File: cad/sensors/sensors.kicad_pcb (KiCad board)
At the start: 2 copper layers, 72 x 50 mm, 4 parts

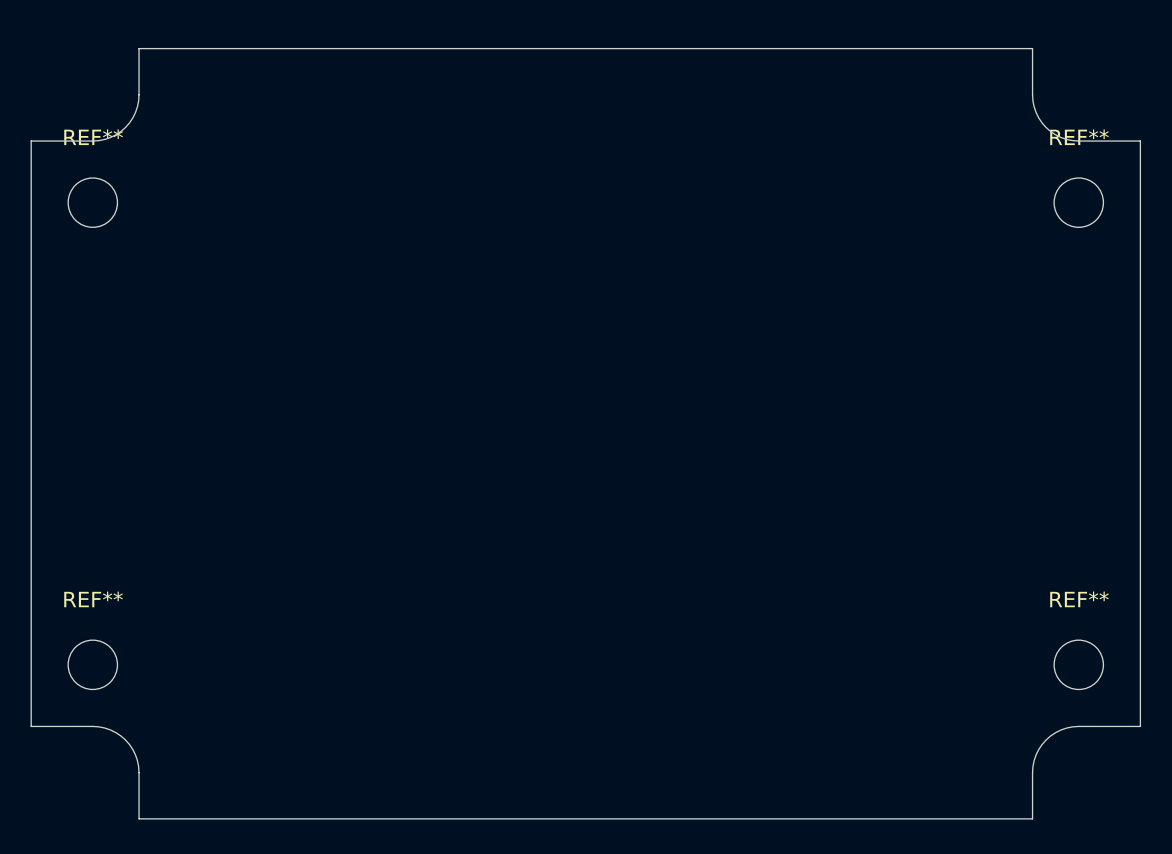
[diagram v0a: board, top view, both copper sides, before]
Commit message: Finished sensor breakout board placement. Ready to begin routing
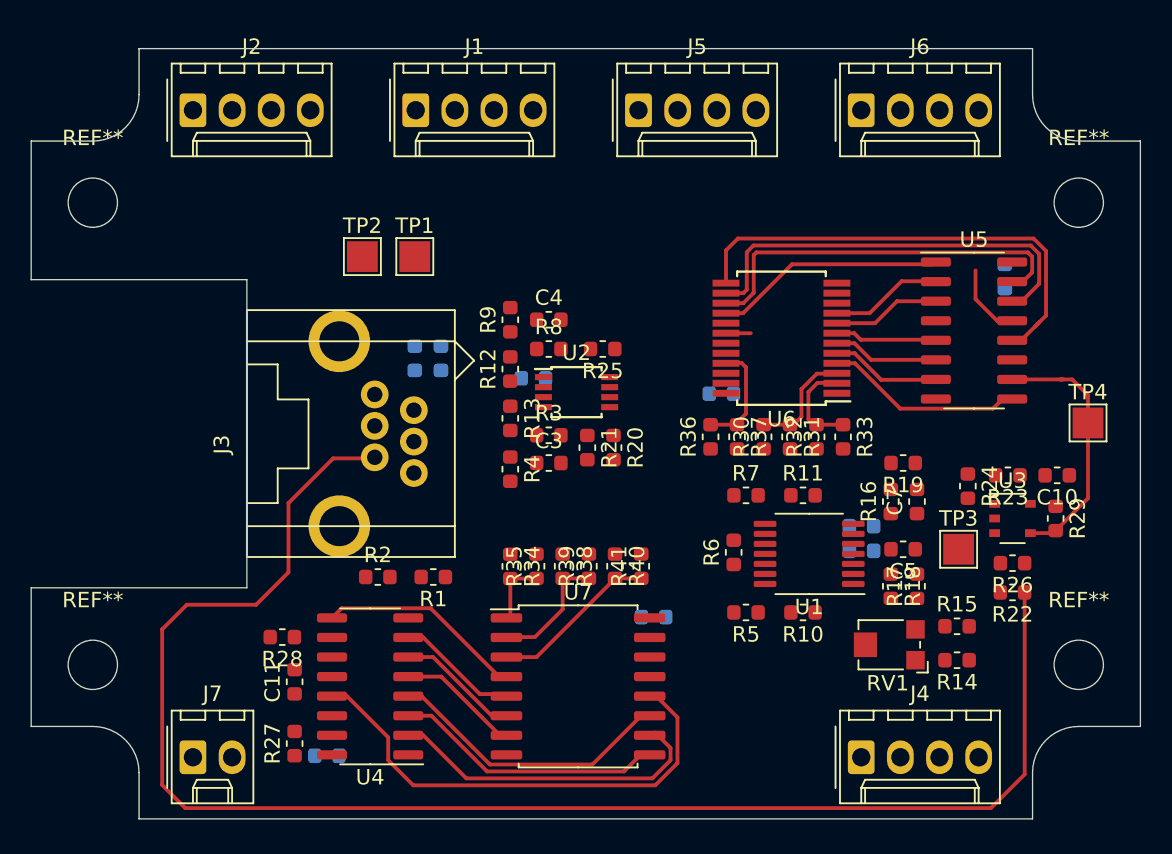
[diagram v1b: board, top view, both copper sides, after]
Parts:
- added C1: 10uF, Capacitor_SMD:C_0603_1608Metric, B.Cu at (120.8, 85.2)
- added C10: 100nF, Capacitor_SMD:C_0603_1608Metric, F.Cu at (162.5, 92.8)
- added C11: 100nF, Capacitor_SMD:C_0603_1608Metric, F.Cu at (113.0, 106.2)
- added C12: 100nF, Capacitor_SMD:C_0603_1608Metric, B.Cu at (140.7, 87.5)
- added C13: 100nF, Capacitor_SMD:C_0603_1608Metric, B.Cu at (115.1, 111.0)
- added C14: 100nF, Capacitor_SMD:C_0603_1608Metric, B.Cu at (136.3, 102.0)
- added C15: 100nF, Capacitor_SMD:C_0603_1608Metric, B.Cu at (159.1, 79.8)
- added C2: 100nF, Capacitor_SMD:C_0603_1608Metric, B.Cu at (122.5, 85.2)
- added C3: DNF, Capacitor_SMD:C_0603_1608Metric, F.Cu at (129.5, 92.0)
- added C4: DNF, Capacitor_SMD:C_0603_1608Metric, F.Cu at (129.5, 82.7)
- added C5: 4.7uF, Capacitor_SMD:C_0603_1608Metric, F.Cu at (152.5, 97.5)
- added C6: 100nF, Capacitor_SMD:C_0603_1608Metric, B.Cu at (128.5, 86.5)
- added C7: 100nF, Capacitor_SMD:C_0603_1608Metric, F.Cu at (153.4, 94.5)
- added C8: 10nF, Capacitor_SMD:C_0603_1608Metric, B.Cu at (149.8, 97.7)
- added C9: 1uF, Capacitor_SMD:C_0603_1608Metric, B.Cu at (149.8, 96.0)
- added J1: Conn_01x04, Connector_Molex:Molex_KK-254_AE-6410-04A_1x04_P2.54mm_Vertical, F.Cu at (120.9, 69.0)
- added J2: Conn_01x04, Connector_Molex:Molex_KK-254_AE-6410-04A_1x04_P2.54mm_Vertical, F.Cu at (106.4, 69.0)
- added J3: 6P6C, custom:E5566-Q0LK22-L, F.Cu at (115.9, 84.0)
- added J4: Conn_01x04, Connector_Molex:Molex_KK-254_AE-6410-04A_1x04_P2.54mm_Vertical, F.Cu at (149.8, 111.0)
- added J5: Conn_01x04, Connector_Molex:Molex_KK-254_AE-6410-04A_1x04_P2.54mm_Vertical, F.Cu at (135.3, 69.0)
- added J6: Conn_01x04, Connector_Molex:Molex_KK-254_AE-6410-04A_1x04_P2.54mm_Vertical, F.Cu at (149.8, 69.0)
- added J7: Conn_01x02, Connector_Molex:Molex_KK-254_AE-6410-02A_1x02_P2.54mm_Vertical, F.Cu at (106.4, 111.0)
- added R1: 0, Resistor_SMD:R_0603_1608Metric, F.Cu at (122.0, 99.3)
- added R10: 1k, Resistor_SMD:R_0603_1608Metric, F.Cu at (146.0, 101.7)
- added R11: 1k, Resistor_SMD:R_0603_1608Metric, F.Cu at (146.0, 94.0)
- added R12: 75, Resistor_SMD:R_0603_1608Metric, F.Cu at (127.0, 85.8)
- added R13: 75, Resistor_SMD:R_0603_1608Metric, F.Cu at (127.0, 89.0)
- added R14: 33k, Resistor_SMD:R_0603_1608Metric, F.Cu at (156.0, 104.8)
- added R15: 33k, Resistor_SMD:R_0603_1608Metric, F.Cu at (156.0, 102.5)
- added R16: 39k, Resistor_SMD:R_0603_1608Metric, F.Cu at (151.7, 94.5)
- added R17: 39k, Resistor_SMD:R_0603_1608Metric, F.Cu at (153.4, 100.0)
- added R18: 0, Resistor_SMD:R_0603_1608Metric, F.Cu at (151.7, 100.0)
- added R19: 1.6k, Resistor_SMD:R_0603_1608Metric, F.Cu at (152.5, 92.0)
- added R2: DNF, Resistor_SMD:R_0603_1608Metric, F.Cu at (118.4, 99.3)
- added R20: 10k, Resistor_SMD:R_0603_1608Metric, F.Cu at (133.7, 91.0)
- added R21: 10k, Resistor_SMD:R_0603_1608Metric, F.Cu at (132.0, 91.0)
- added R22: DNF, Resistor_SMD:R_0603_1608Metric, F.Cu at (159.6, 100.3)
- added R23: 100k, Resistor_SMD:R_0603_1608Metric, F.Cu at (159.3, 92.8)
- added R24: 100k, Resistor_SMD:R_0603_1608Metric, F.Cu at (156.7, 93.5)
- added R25: 10k, Resistor_SMD:R_0603_1608Metric, F.Cu at (133.0, 84.5)
- added R26: 775k, Resistor_SMD:R_0603_1608Metric, F.Cu at (159.6, 98.5)
- added R27: 10k, Resistor_SMD:R_0603_1608Metric, F.Cu at (113.0, 110.2)
- added R28: 100k, Resistor_SMD:R_0603_1608Metric, F.Cu at (112.2, 103.2)
- added R29: 10k, Resistor_SMD:R_0603_1608Metric, F.Cu at (162.4, 95.5)
- added R3: 2.2k, Resistor_SMD:R_0603_1608Metric, F.Cu at (129.5, 90.2)
- added R30: DNF, Resistor_SMD:R_0603_1608Metric, F.Cu at (143.4, 90.2)
- added R31: 0, Resistor_SMD:R_0603_1608Metric, F.Cu at (145.2, 90.2)
- added R32: DNF, Resistor_SMD:R_0603_1608Metric, F.Cu at (146.9, 90.2)
- added R33: 0, Resistor_SMD:R_0603_1608Metric, F.Cu at (148.6, 90.2)
- added R34: DNF, Resistor_SMD:R_0603_1608Metric, F.Cu at (127.0, 98.7)
- added R35: 0, Resistor_SMD:R_0603_1608Metric, F.Cu at (128.7, 98.7)
- added R36: DNF, Resistor_SMD:R_0603_1608Metric, F.Cu at (140.0, 90.2)
- added R37: 0, Resistor_SMD:R_0603_1608Metric, F.Cu at (141.7, 90.2)
- added R38: DNF, Resistor_SMD:R_0603_1608Metric, F.Cu at (130.4, 98.7)
- added R39: 0, Resistor_SMD:R_0603_1608Metric, F.Cu at (132.1, 98.7)
- added R4: DNF, Resistor_SMD:R_0603_1608Metric, F.Cu at (127.0, 92.3)
- added R40: DNF, Resistor_SMD:R_0603_1608Metric, F.Cu at (133.8, 98.7)
- added R41: 0, Resistor_SMD:R_0603_1608Metric, F.Cu at (135.5, 98.7)
- added R5: 0, Resistor_SMD:R_0603_1608Metric, F.Cu at (142.3, 101.7)
- added R6: DNF, Resistor_SMD:R_0603_1608Metric, F.Cu at (141.5, 97.8)
- added R7: 0, Resistor_SMD:R_0603_1608Metric, F.Cu at (142.3, 94.0)
- added R8: 2.2k, Resistor_SMD:R_0603_1608Metric, F.Cu at (129.5, 84.5)
- added R9: DNF, Resistor_SMD:R_0603_1608Metric, F.Cu at (127.0, 82.7)
- added RV1: 10k, Potentiometer_SMD:Potentiometer_Bourns_TC33X_Vertical, F.Cu at (151.5, 103.8)
- added TP1: RCU-0C, TestPoint:TestPoint_Pad_2.0x2.0mm, F.Cu at (120.8, 78.5)
- added TP2: RCU-0C, TestPoint:TestPoint_Pad_2.0x2.0mm, F.Cu at (117.4, 78.5)
- added TP3: RCU-0C, TestPoint:TestPoint_Pad_2.0x2.0mm, F.Cu at (156.1, 97.5)
- added TP4: RCU-0C, TestPoint:TestPoint_Pad_2.0x2.0mm, F.Cu at (164.5, 89.3)
- added U1: LMV324, Package_SO:TSSOP-14_4.4x5mm_P0.65mm, F.Cu at (146.4, 97.8)
- added U2: PCA9517A, Package_SO:TSSOP-8_3x3mm_P0.65mm, F.Cu at (131.3, 87.3)
- added U3: LMV331, Package_SO:TSOP-5_1.65x3.05mm_P0.95mm, F.Cu at (159.6, 95.5)
- added U4: MC14040B, Package_SO:SOIC-16_3.9x9.9mm_P1.27mm, F.Cu at (117.9, 106.5)
- added U5: MC14040B, Package_SO:SOIC-16_3.9x9.9mm_P1.27mm, F.Cu at (157.1, 83.3)
- added U6: TCA9555DBR, Package_SO:SSOP-24_5.3x8.2mm_P0.65mm, F.Cu at (144.6, 83.8)
- added U7: PCF8574, Package_SO:SOIC-16W_7.5x10.3mm_P1.27mm, F.Cu at (131.4, 106.5)
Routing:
- net /ADC: track 0.00 -> 100.4 mm
- net Net-(U4-Pad13): track 0.00 -> 31.4 mm
- net Net-(U5-Pad12): track 0.00 -> 30.5 mm
- net Net-(U5-Pad14): track 0.00 -> 26.9 mm
- net Net-(U5-Pad15): track 0.00 -> 24.8 mm
- net Net-(U4-Pad2): track 0.00 -> 20.9 mm
- net Net-(U4-Pad4): track 0.00 -> 18.1 mm
- net Net-(U4-Pad3): track 0.00 -> 16.9 mm
- net Net-(R26-Pad1): track 0.00 -> 16.1 mm
- net Net-(U5-Pad1): track 0.00 -> 14.7 mm
- net Net-(U4-Pad9): track 0.00 -> 13.1 mm
- net Net-(U5-Pad9): track 0.00 -> 12.3 mm
- net Net-(R40-Pad2): track 0.00 -> 10.8 mm
- net Net-(U4-Pad6): track 0.00 -> 8.14 mm
- net Net-(U4-Pad7): track 0.00 -> 8.05 mm
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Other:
- outline, holes or cut-outs redrawn

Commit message: Finished routing sensor breakout board. Need to draw power planes
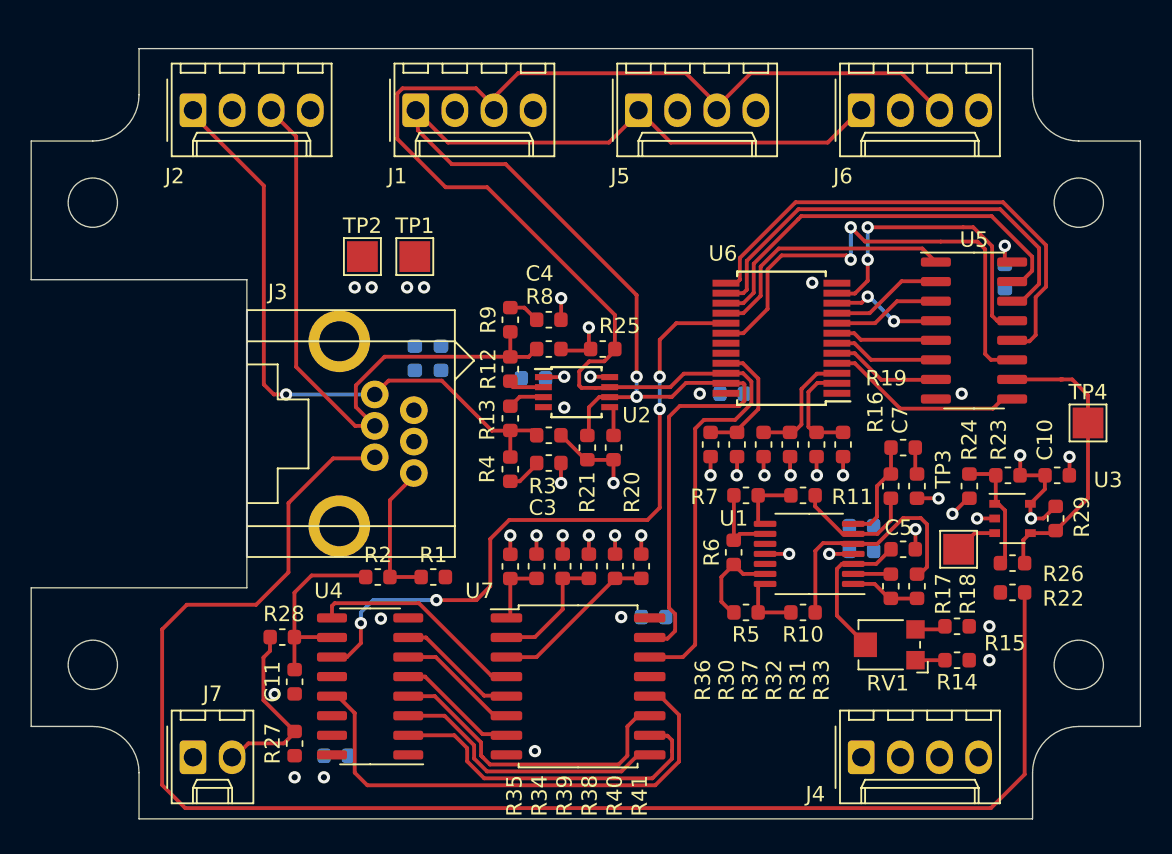
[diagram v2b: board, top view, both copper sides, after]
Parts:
- moved C7 1.00 mm to (153.4, 93.5)
- moved R16 1.00 mm to (151.7, 93.5)
- moved R19 1.00 mm to (152.5, 91.0)
- moved C12 0.70 mm to (141.4, 87.5), turned to 180 degrees
- moved C13 0.60 mm to (115.7, 111.0), turned to 180 degrees
- moved R30 0.50 mm to (143.4, 90.8)
- moved R31 0.50 mm to (145.2, 90.8)
- moved R32 0.50 mm to (146.9, 90.8)
- moved R33 0.50 mm to (148.6, 90.8)
- moved R36 0.50 mm to (140.0, 90.8)
- moved R37 0.50 mm to (141.7, 90.8)
- moved R24 0.10 mm to (156.8, 93.5)
- turned R1 to 0 degrees
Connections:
- J1 pad 1: /SDA_BUF -> /SDA
- J1 pad 3: /SCL_BUF -> /SCL
- J2 pad 1: /SDA_BUF -> /SDA_RJ11
- J2 pad 3: /SCL_BUF -> /SCL_RJ11
- J3 pad 4: /SCL_BUF -> /SCL_RJ11
- J3 pad 6: /SDA_BUF -> /SDA_RJ11
- R1 pad 1: GND -> Net-(J3-Pad1)
- R1 pad 2: Net-(J3-Pad1) -> GND
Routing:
- net /SCL: track 0.00 -> 103.4 mm
- net /SDA: track 0.00 -> 94.3 mm, vias 0 -> 2
- net /RG_CLR: track 0.00 -> 43.9 mm, vias 0 -> 4
- net /SCL_RJ11: track 0.00 -> 41.5 mm
- net /SDA_RJ11: track 0.00 -> 41.1 mm, vias 0 -> 1
- net /AN_CLR: track 1.61 -> 31.5 mm, vias 0 -> 2
- net /3V3: track 0.00 -> 28.7 mm, vias 0 -> 20
- net GND: track 0.00 -> 17.7 mm, vias 0 -> 24
- net Net-(U5-Pad13): track 4.82 -> 20.4 mm, vias 0 -> 2
- net Net-(R10-Pad1): track 0.00 -> 15.5 mm
- net /RAIN_TRG: track 0.00 -> 12.5 mm
- net Net-(J7-Pad2): track 0.00 -> 11.5 mm
- net Net-(C5-Pad2): track 0.00 -> 9.60 mm
- net Net-(J3-Pad1): track 0.00 -> 9.18 mm
- net Net-(R11-Pad2): track 0.00 -> 8.51 mm
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
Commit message: Begain routing planes on sensor board
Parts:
- moved R34 0.60 mm to (127.0, 99.3)
- moved R35 0.60 mm to (128.7, 99.2)
- moved R38 0.60 mm to (130.4, 99.2)
- moved R39 0.60 mm to (132.1, 99.2)
- moved R40 0.60 mm to (133.8, 99.2)
- moved R41 0.60 mm to (135.5, 99.2)
- moved R6 0.32 mm to (141.4, 98.0)
- moved R30 0.30 mm to (143.4, 90.5)
- moved R31 0.30 mm to (145.2, 90.5)
- moved R32 0.30 mm to (146.9, 90.5)
- moved R33 0.30 mm to (148.6, 90.5)
- moved R36 0.30 mm to (140.0, 90.5)
- moved R37 0.30 mm to (141.7, 90.5)
- moved R7 0.22 mm to (142.1, 94.2)
- moved R5 0.20 mm to (142.1, 101.7)
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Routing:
- net /3V3: track 28.7 -> 155.7 mm, vias 20 -> 13
- net Net-(J4-Pad3): track 0.00 -> 21.7 mm, vias 0 -> 2
- net Net-(J4-Pad2): track 0.00 -> 21.4 mm, vias 0 -> 2
- net /RG_CLR: track 43.9 -> 47.9 mm
- net Net-(R10-Pad1): track 15.5 -> 11.7 mm
- net Net-(R34-Pad2): track 4.10 -> 1.80 mm
- net /SDA: track 94.3 -> 92.5 mm
- net GND: track 17.7 -> 16.2 mm, vias 24 -> 27
- net Net-(R11-Pad1): track 3.70 -> 5.08 mm
- net /SCL: track 103.4 -> 104.3 mm
- net Net-(R11-Pad2): track 8.51 -> 9.29 mm
- net Net-(R6-Pad2): track 4.77 -> 5.50 mm
- net Net-(R38-Pad2): track 7.65 -> 7.03 mm
- net (no net): vias 0 -> 2
- added copper zone on B.Cu, net /3V3

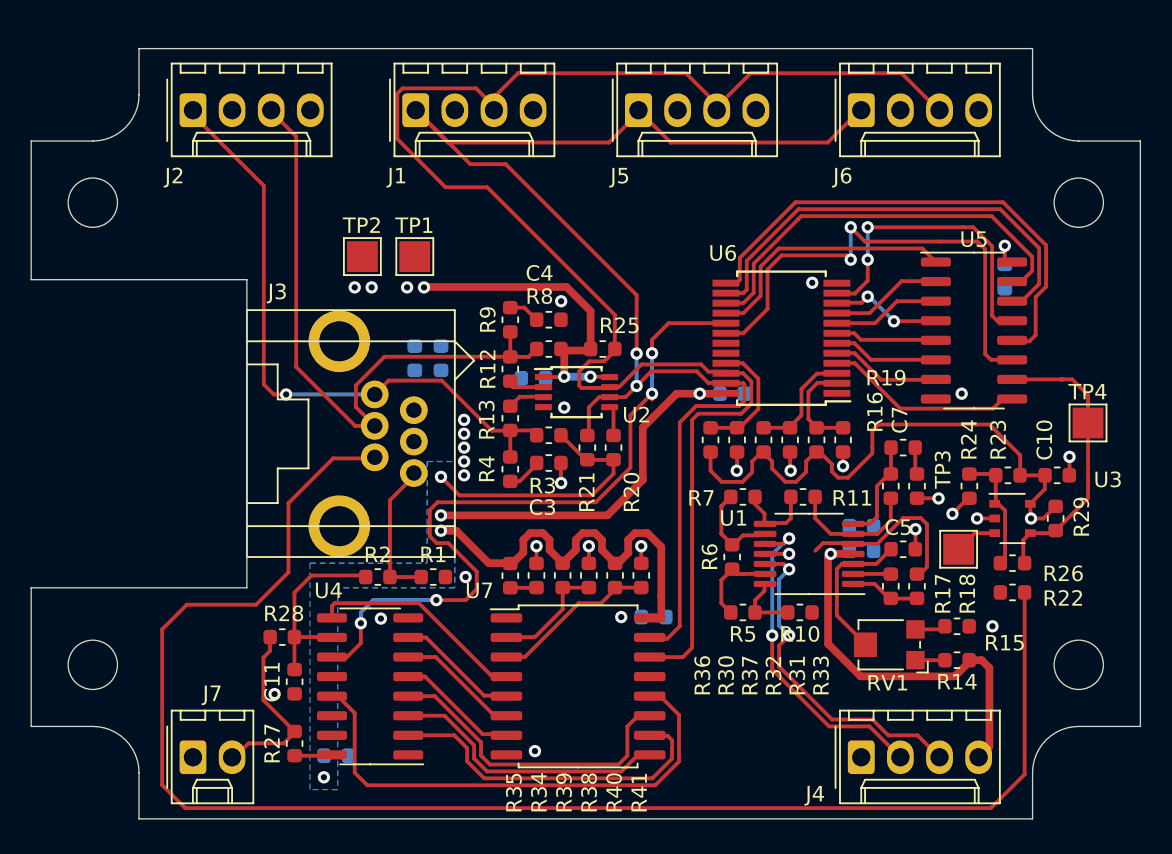
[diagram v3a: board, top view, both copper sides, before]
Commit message: routing power planes on sensor board
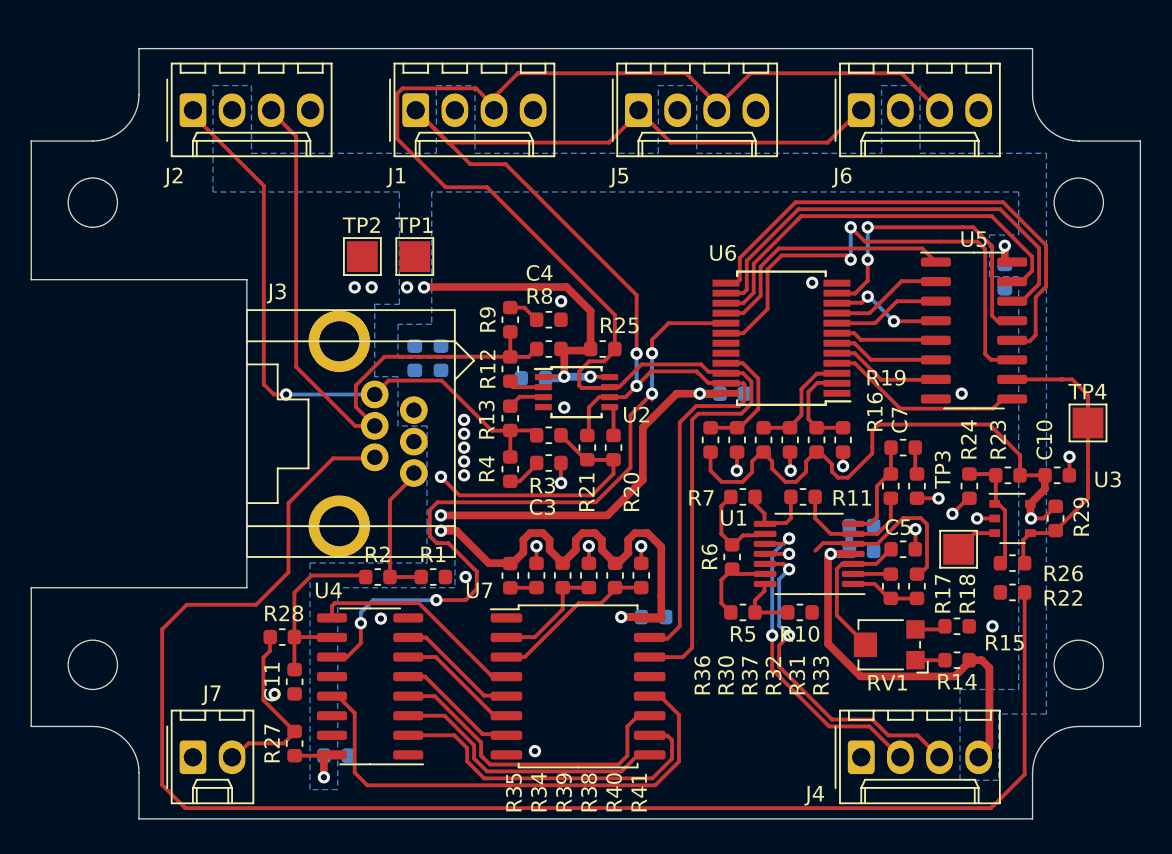
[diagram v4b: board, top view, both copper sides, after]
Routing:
- net /3V3: track 155.7 -> 165.8 mm
- net GND: vias 27 -> 29
- net (no net): vias 2 -> 0

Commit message: Finished sensor board layout
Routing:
- net Net-(C7-Pad2): track 3.37 -> 14.0 mm
- net GND: track 16.2 -> 8.09 mm, vias 29 -> 80
- net Net-(R10-Pad1): track 11.7 -> 15.5 mm
- net /SCL: track 104.3 -> 107.7 mm
- net Net-(R34-Pad2): track 1.80 -> 3.80 mm
- net /3V3: track 165.8 -> 167.6 mm
- net /SDA: track 92.5 -> 94.1 mm
- net /ADC: track 100.4 -> 99.5 mm
- net (no net): vias 0 -> 3
- added copper zone on F.Cu, net /3V3
- added copper zone on B.Cu, net GND
- added copper zone on F.Cu, net GND

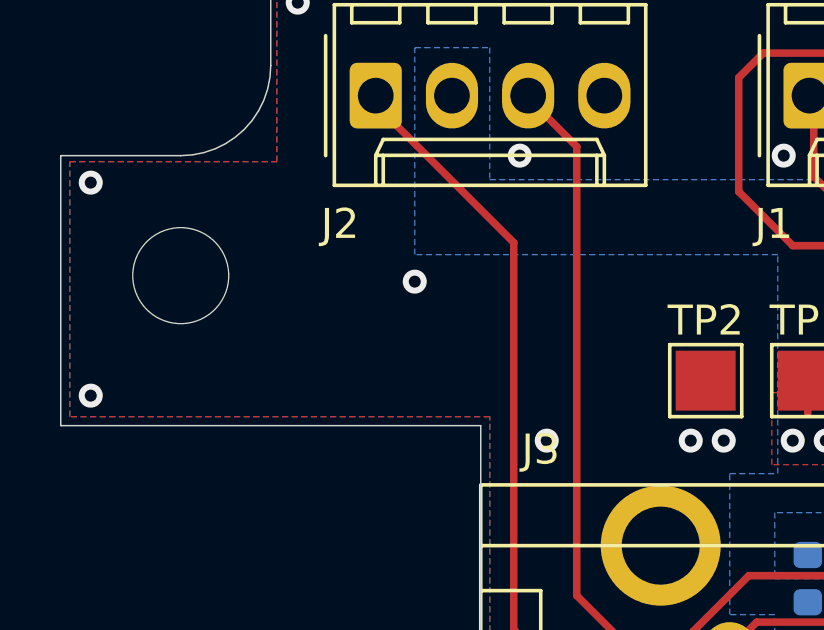
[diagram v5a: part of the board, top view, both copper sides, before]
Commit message: Finished routing wind sensor(s) board
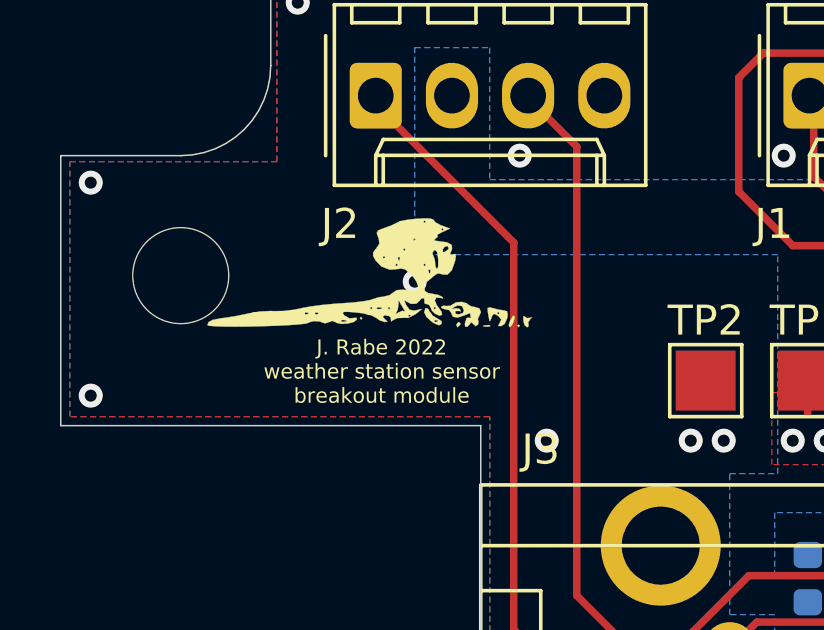
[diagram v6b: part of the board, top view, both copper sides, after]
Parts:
- added G***: LOGO, custom:logo_JR_3, F.Cu at (106.8, 74.7)
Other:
- board text added: "J. Rabe 2022 weather station sensor breakout module"
